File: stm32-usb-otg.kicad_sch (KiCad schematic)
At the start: 40 parts

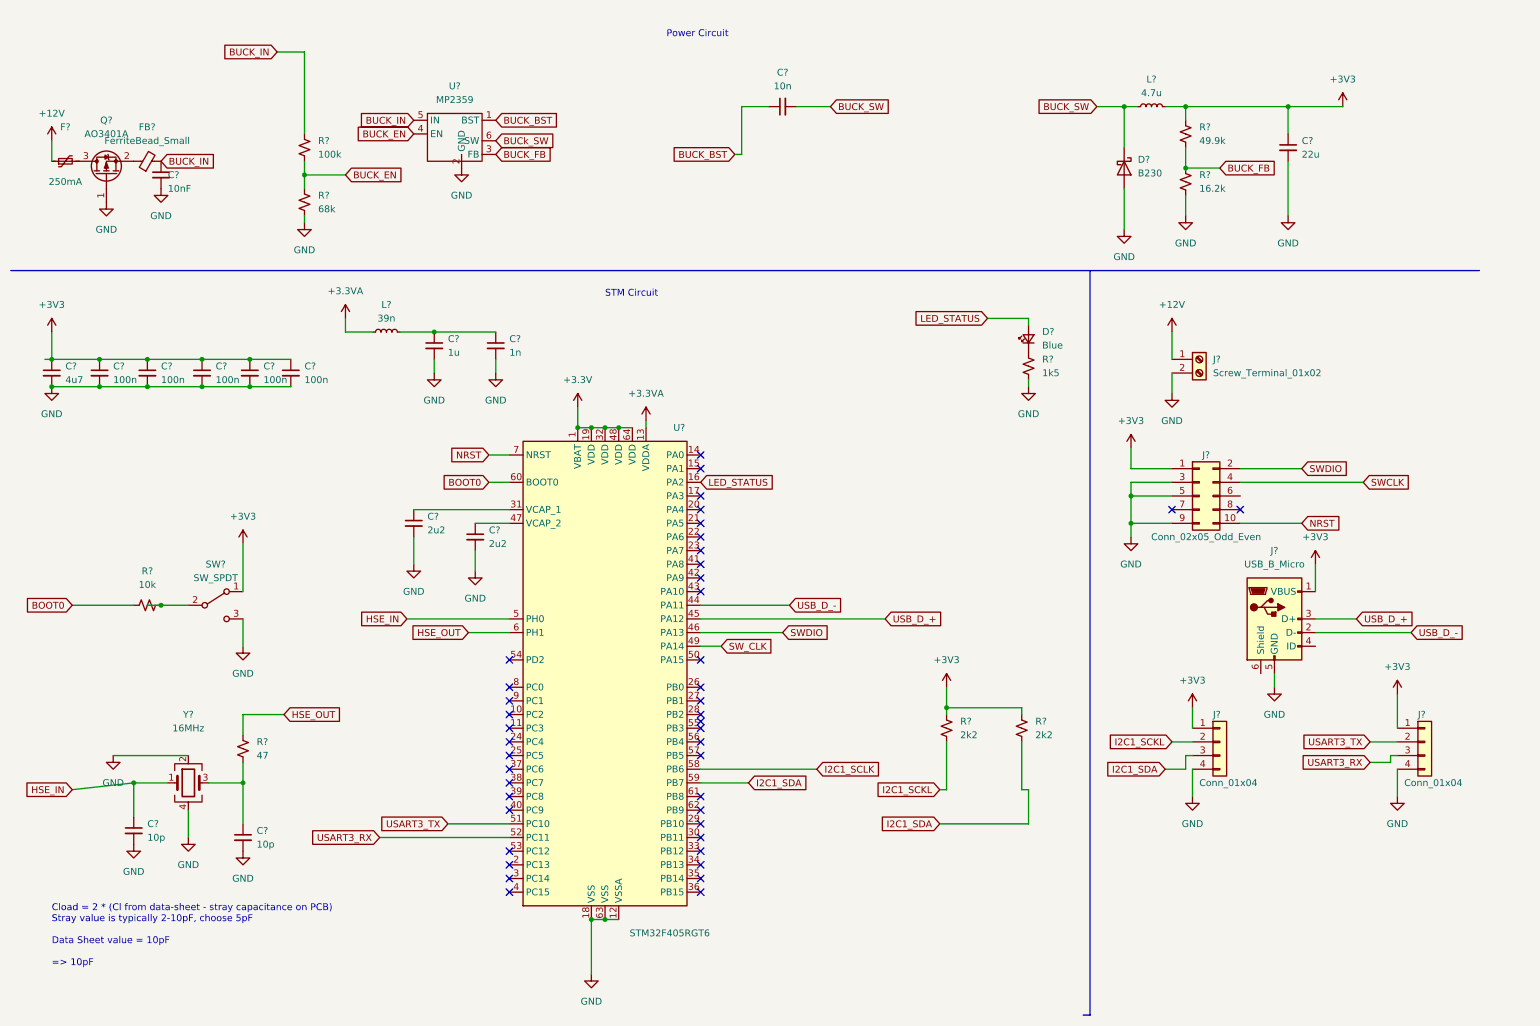
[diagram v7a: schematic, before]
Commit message: Added USB TVS protection.
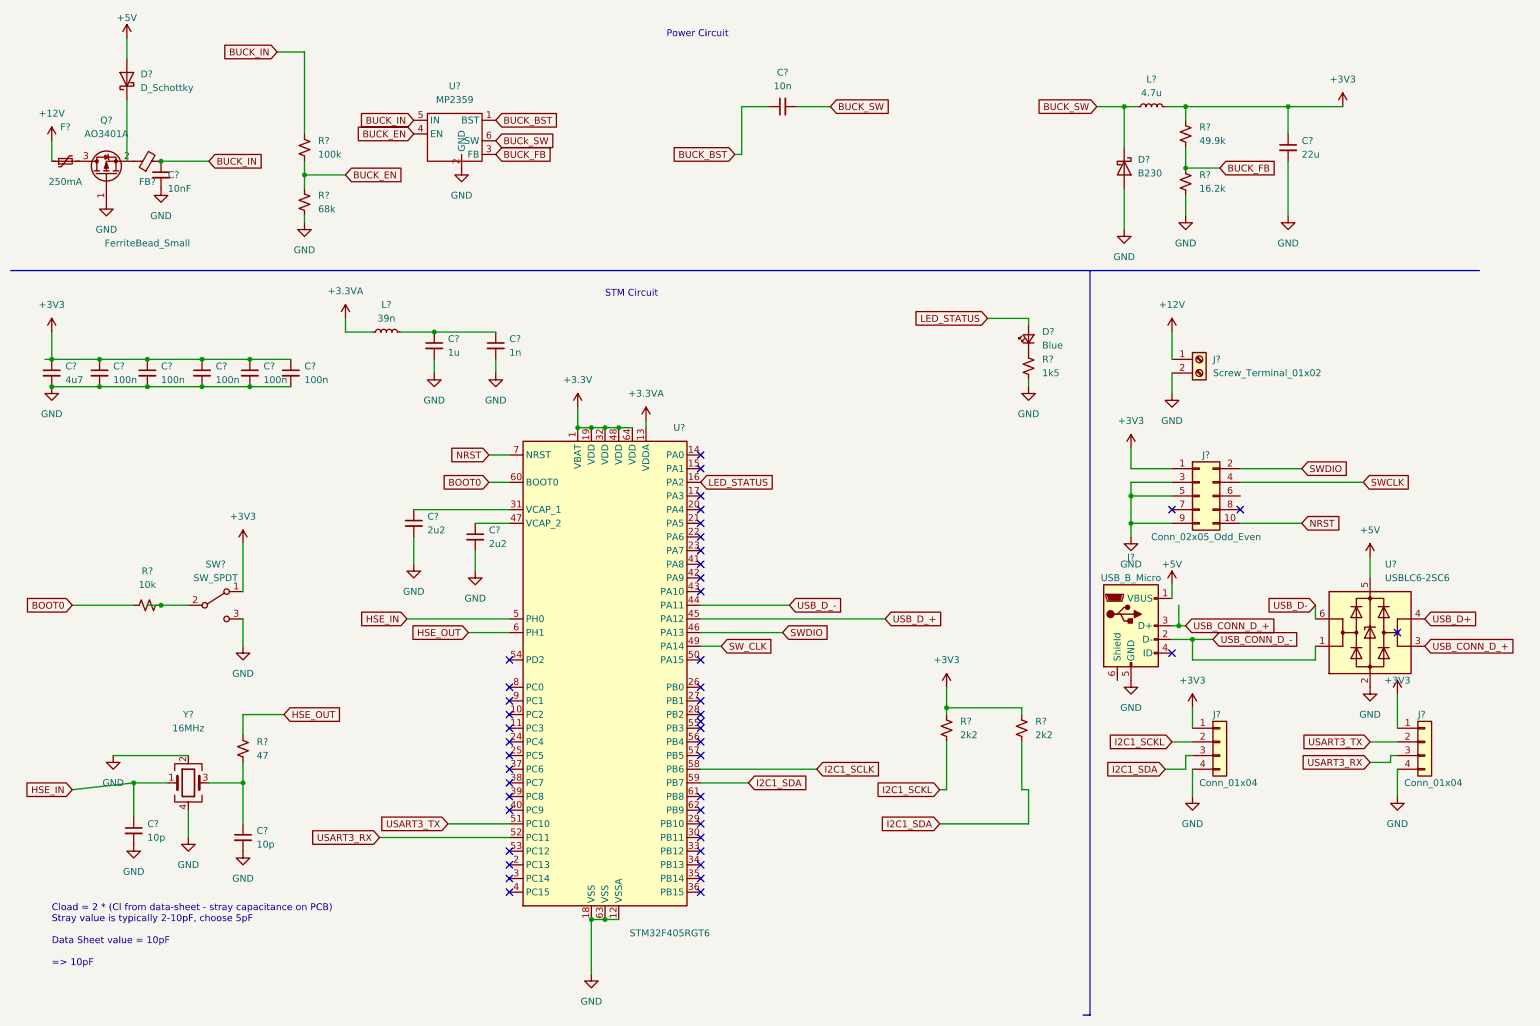
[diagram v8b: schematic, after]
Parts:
- added D?: D_Schottky, symbol Device:D_Schottky
- added U?: USBLC6-2SC6, Package_TO_SOT_SMD:SOT-23-6, symbol Power_Protection:USBLC6-2SC6
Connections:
- net +3V3: no longer J?.1 (VBUS)
- net GND: now also U?.2 (GND)
- net USB_D_+: no longer J?.3 (D+)
- net USB_D_-: no longer J?.2 (D-)
- new net +5V: D?.2 (A), J?.1 (VBUS), U?.5 (VBUS)
- new net USB_CONN_D_+: J?.3 (D+), U?.3 (I/O2)
- new net USB_CONN_D_-: J?.2 (D-), U?.1 (I/O1)
- new net USB_D+: U?.4 (I/O2)
- new net USB_D-: U?.6 (I/O1)
- no-connect marks 43 -> 45
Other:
- moved on the sheet: J?
